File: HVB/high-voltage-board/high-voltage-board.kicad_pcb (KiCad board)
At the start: 2 copper layers, 181.6 x 105.4 mm, 69 parts, among them J1 Conn_01x23, J10 Conn_01x05, J11 HV-, J2 HECS, J3 HV+, J4 HV-, J5 HV+, J6 HV-, J7 Conn_01x02, J8 HV+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

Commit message: updating trace correction temp
changing trace and pinout of a temp wire
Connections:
- U5 pad 17: unconnected-(U5-Pad17) -> /TEMP-
- U5 pad 29: /TEMP- -> unconnected-(U5-Pad29)
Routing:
- net /TEMP-: track 10.2 -> 11.8 mm

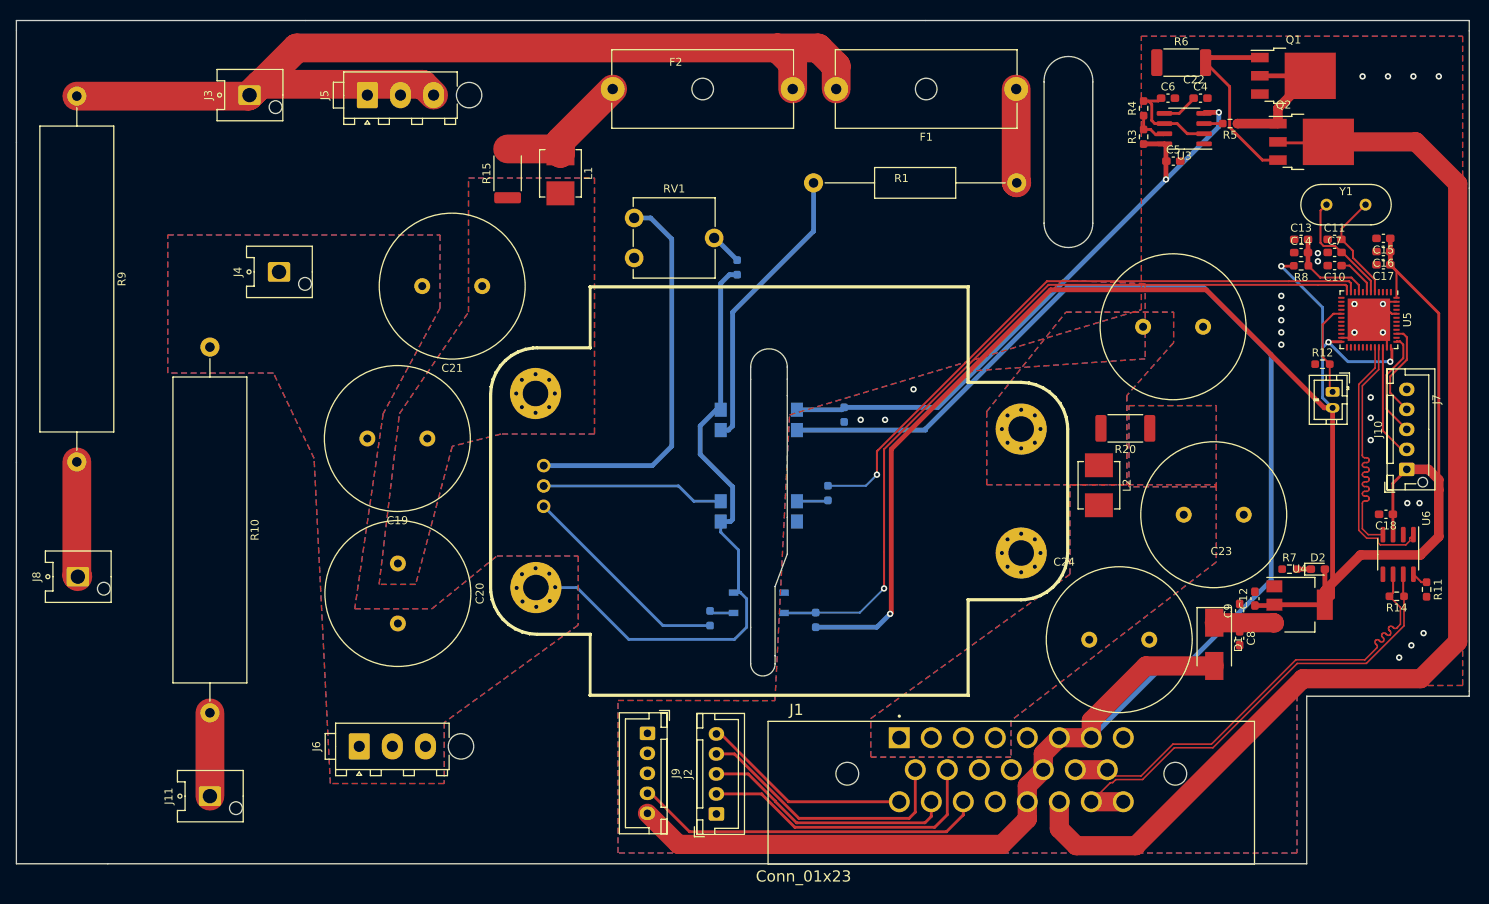
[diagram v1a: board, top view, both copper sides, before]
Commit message: adding mounting holes
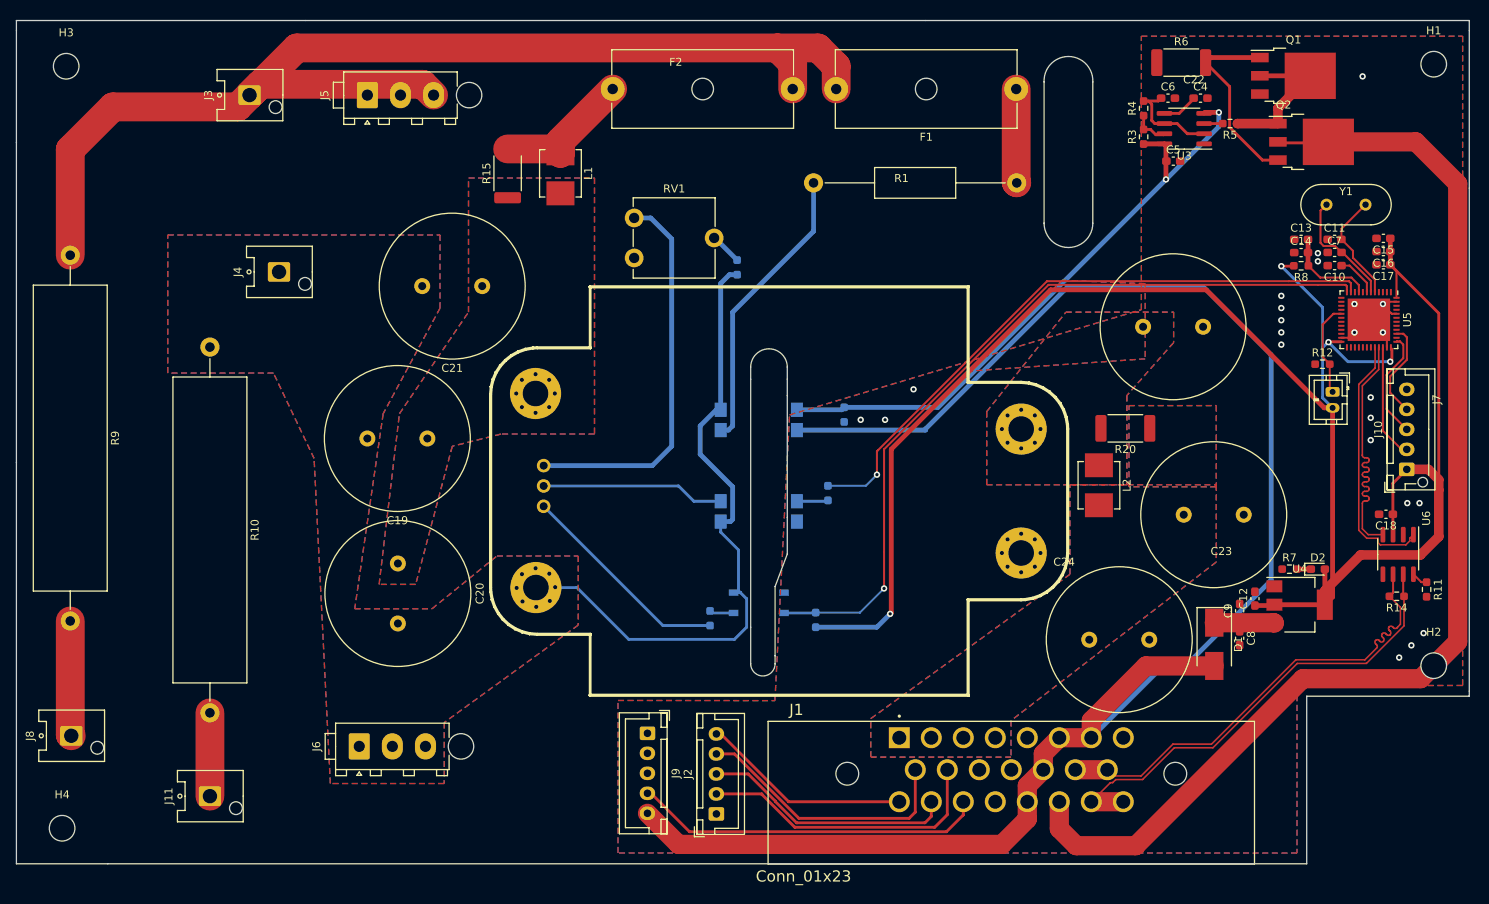
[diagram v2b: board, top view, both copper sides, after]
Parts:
- added H1: MountingHole, MountingHole:MountingHole_3.2mm_M3, F.Cu at (224.8, 44.2)
- added H2: MountingHole, MountingHole:MountingHole_3.2mm_M3, F.Cu at (224.8, 119.4)
- added H3: MountingHole, MountingHole:MountingHole_3.2mm_M3, F.Cu at (53.8, 44.5)
- added H4: MountingHole, MountingHole:MountingHole_3.2mm_M3, F.Cu at (53.3, 139.7)
- moved J8 19.9 mm to (54.5, 128.1)
- moved R9 19.9 mm to (54.4, 68.1)
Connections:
- U5 pad 10: /DC_DC_TRIM_EN -> unconnected-(U5-Pad10)
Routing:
- net HV+: track 131.3 -> 148.1 mm
- net GND: vias 26 -> 23
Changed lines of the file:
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@@
   (net 41 "unconnected-(U5-Pad4)")
   (net 42 "unconnected-(U5-Pad8)")
-  (net 43 "/DC_DC_TRIM_EN")
+  (net 43 "unconnected-(U5-Pad10)")
   (net 44 "unconnected-(U5-Pad42)")
   (net 45 "unconnected-(U5-Pad43)")
@@
     )
   )
+  (footprint "MountingHole:MountingHole_3.2mm_M3" (layer "F.Cu")
+    (at 53.34 139.7)
+    (descr "Mounting Hole 3.2mm, no annular, M3")
+    (tags "mounting hole 3.2mm no annular m3")
+    (property "Sheetfile" "high-voltage-board.kicad_sch")
+    (property "Sheetname" "")
+    (attr exclude_from_pos_files)
+    (fp_text reference "H4" (at 0 -4.2) (layer "F.SilkS")
+      (effects (font (size 1 1) (thickness 0.15)))
+    )
+    (fp_text value "MountingHole" (at 0 4.2) (layer "F.Fab")
+      (effects (font (size 1 1) (thickness 0.15)))
+    )
+    (fp_text user "${REFERENCE}" (at 0.3 0) (layer "F.Fab")
+      (effects (font (size 1 1) (thickness 0.15)))
+    )
+    (fp_circle (center 0 0) (end 3.2 0) (layer "Cmts.User") (width 0.15) (fill none))
+    (fp_circle (center 0 0) (end 3.45 0) (layer "F.CrtYd") (width 0.05) (fill none))
+    (pad "" np_thru_hole circle (at 0 0) (size 3.2 3.2) (drill 3.2) (layers *.Cu *.Mask))
+  )
   (footprint "Connector_Hirose:Hirose_DF63M-1P-3.96DSA_1x01_P3.96mm_Vertical" (layer "F.Cu")
     (at 71.8157 135.6891 90)
@@
     )
   )
+  (footprint "MountingHole:MountingHole_3.2mm_M3" placed (layer "F.Cu")
+    (at 224.79 119.38)
+    (descr "Mounting Hole 3.2mm, no annular, M3")
+    (tags "mounting hole 3.2mm no annular m3")
+    (property "Sheetfile" "high-voltage-board.kicad_sch")
+    (property "Sheetname" "")
+    (attr exclude_from_pos_files)
+    (fp_text reference "H2" (at 0 -4.2) (layer "F.SilkS")
+      (effects (font (size 1 1) (thickness 0.15)))
+    )
+    (fp_text value "MountingHole" (at 0 4.2) (layer "F.Fab")
+      (effects (font (size 1 1) (thickness 0.15)))
+    )
+    (fp_text user "${REFERENCE}" (at 0.3 0) (layer "F.Fab")
+      (effects (font (size 1 1) (thickness 0.15)))
+    )
+    (fp_circle (center 0 0) (end 3.2 0) (layer "Cmts.User") (width 0.15) (fill none))
+    (fp_circle (center 0 0) (end 3.45 0) (layer "F.CrtYd") (width 0.05) (fill none))
+    (pad "" np_thru_hole circle (at 0 0) (size 3.2 3.2) (drill 3.2) (layers *.Cu *.Mask))
+  )
   (footprint "LED_SMD:LED_0603_1608Metric_Pad1.05x0.95mm_HandSolder" (layer "F.Cu")
     (at 210.312 107.315)
@@
     )
   )
+  (footprint "MountingHole:MountingHole_3.2mm_M3" placed (layer "F.Cu")
+    (at 53.848 44.45)
+    (descr "Mounting Hole 3.2mm, no annular, M3")
+    (tags "mounting hole 3.2mm no annular m3")
+    (property "Sheetfile" "high-voltage-board.kicad_sch")
+    (property "Sheetname" "")
+    (attr exclude_from_pos_files)
+    (fp_text reference "H3" (at 0 -4.2) (layer "F.SilkS")
+      (effects (font (size 1 1) (thickness 0.15)))
+    )
+    (fp_text value "MountingHole" (at 0 4.2) (layer "F.Fab")
+      (effects (font (size 1 1) (thickness 0.15)))
+    )
+    (fp_text user "${REFERENCE}" (at 0.3 0) (layer "F.Fab")
+      (effects (font (size 1 1) (thickness 0.15)))
+    )
+    (fp_circle (center 0 0) (end 3.2 0) (layer "Cmts.User") (width 0.15) (fill none))
+    (fp_circle (center 0 0) (end 3.45 0) (layer "F.CrtYd") (width 0.05) (fill none))
+    (pad "" np_thru_hole circle (at 0 0) (size 3.2 3.2) (drill 3.2) (layers *.Cu *.Mask))
+  )
   (footprint "Package_TO_SOT_SMD:TO-252-3_TabPin2" (layer "F.Cu")
     (at 209.5187 53.9021)
@@
     )
   )
+  (footprint "MountingHole:MountingHole_3.2mm_M3" placed (layer "F.Cu")
+    (at 224.79 44.196)
+    (descr "Mounting Hole 3.2mm, no annular, M3")
+    (tags "mounting hole 3.2mm no annular m3")
+    (property "Sheetfile" "high-voltage-board.kicad_sch")
+    (property "Sheetname" "")
+    (attr exclude_from_pos_files)
+    (fp_text reference "H1" (at 0 -4.2) (layer "F.SilkS")
+      (effects (font (size 1 1) (thickness 0.15)))
+    )
+    (fp_text value "MountingHole" (at 0 4.2) (layer "F.Fab")
+      (effects (font (size 1 1) (thickness 0.15)))
+    )
+    (fp_text user "${REFERENCE}" (at 0.3 0) (layer "F.Fab")
+      (effects (font (size 1 1) (thickness 0.15)))
+    )
+    (fp_circle (center 0 0) (end 3.2 0) (layer "Cmts.User") (width 0.15) (fill none))
+    (fp_circle (center 0 0) (end 3.45 0) (layer "F.CrtYd") (width 0.05) (fill none))
+    (pad "" np_thru_hole circle (at 0 0) (size 3.2 3.2) (drill 3.2) (layers *.Cu *.Mask))
+  )
   (footprint "Capacitor_SMD:C_0603_1608Metric_Pad1.08x0.95mm_HandSolder" (layer "F.Cu")
     (at 192.2382 56.3141)
@@
   )
   (footprint "Resistor_THT:R_Axial_Power_L38.0mm_W9.0mm_P45.72mm" (layer "F.Cu")
-    (at 55.1787 48.1861 -90)
+    (at 54.356 68.072 -90)
     (descr "Resistor, Axial_Power series, Box, pin pitch=45.72mm, 9W, length*width*height=38*9*9mm^3, http://cdn-reichelt.de/documents/datenblatt/B400/5WAXIAL_9WAXIAL_11WAXIAL_17WAXIAL%23YAG.pdf")
     (tags "Resistor Axial_Power series Box pin pitch 45.72mm 9W length 38mm width 9mm height 9mm")
@@
       (net 11 "Net-(C13-Pad2)") (pinfunction "VDDA") (pintype "power_in"))
     (pad "10" smd roundrect (at -3.45 1.75 270) (size 0.8 0.25) (layers "F.Cu" "F.Paste" "F.Mask") (roundrect_rratio 0.25)
-      (net 43 "/DC_DC_TRIM_EN") (pinfunction "PA0") (pintype "bidirectional"))
+      (net 43 "unconnected-(U5-Pad10)") (pinfunction "PA0") (pintype "bidirectional"))
     (pad "11" smd roundrect (at -3.45 2.25 270) (size 0.8 0.25) (layers "F.Cu" "F.Paste" "F.Mask") (roundrect_rratio 0.25)
       (net 35 "/DC_DC_EN") (pinfunction "PA1") (pintype "bidirectional"))
@@
   )
   (footprint "Connector_Hirose:Hirose_DF63M-1P-3.96DSA_1x01_P3.96mm_Vertical" (layer "F.Cu")
-    (at 55.3057 108.2571 90)
+    (at 54.483 128.143 90)
     (descr "Hirose DF63 through hole, DF63M-1P-3.96DSA, 1 Pins per row (https://www.hirose.com/product/en/products/DF63/), generated with kicad-footprint-generator")
     (tags "connector Hirose DF63 vertical")
@@
   (segment (start 218.9377 79.5876) (end 218.9377 78.6876) (width 0.254) (layer "F.Cu") (net 2))
   (segment (start 219.5377 75.3876) (end 219.0877 74.9376) (width 0.254) (layer "F.Cu") (net 2))
-  (via (at 222.25 45.72) (size 0.8) (drill 0.4) (layers "F.Cu" "B.Cu") (free) (net 2))
   (via (at 218.44 74.168) (size 0.8) (drill 0.4) (layers "F.Cu" "B.Cu") (net 2))
   (via (at 223.52 115.316) (size 0.8) (drill 0.4) (layers "F.Cu" "B.Cu") (free) (net 2))
@@
   (via (at 205.74 79.248) (size 0.8) (drill 0.4) (layers "F.Cu" "B.Cu") (free) (net 2))
   (via (at 218.44 77.724) (size 0.8) (drill 0.4) (layers "F.Cu" "B.Cu") (net 2))
-  (via (at 219.075 45.72) (size 0.8) (drill 0.4) (layers "F.Cu" "B.Cu") (free) (net 2))
   (via (at 214.884 74.168) (size 0.8) (drill 0.4) (layers "F.Cu" "B.Cu") (net 2))
   (via (at 215.9 45.72) (size 0.8) (drill 0.4) (layers "F.Cu" "B.Cu") (free) (net 2))
@@
   (via (at 205.74 73.152) (size 0.8) (drill 0.4) (layers "F.Cu" "B.Cu") (free) (net 2))
   (via (at 216.916 88.392) (size 0.8) (drill 0.4) (layers "F.Cu" "B.Cu") (free) (net 2))
-  (via (at 225.425 45.72) (size 0.8) (drill 0.4) (layers "F.Cu" "B.Cu") (free) (net 2))
   (via (at 153.162 88.646) (size 0.8) (drill 0.4) (layers "F.Cu" "B.Cu") (free) (net 2))
   (via (at 156.21 88.646) (size 0.8) (drill 0.4) (layers "F.Cu" "B.Cu") (free) (net 2))
@@
   (segment (start 137.7188 70.5085) (end 136.7555 70.5085) (width 0.6) (layer "B.Cu") (net 61))
   (segment (start 138.1417 110.2521) (end 137.8877 109.9981) (width 0.36) (layer "B.Cu") (net 61))
-  (segment (start 55.1787 48.1861) (end 76.6417 48.1861) (width 3.6) (layer "F.Cu") (net 62))
+  (segment (start 59.69 49.53) (end 54.356 54.864) (width 3.6) (layer "F.Cu") (net 62))
   (segment (start 82.6638 42.164) (end 142.748 42.164) (width 3.6) (layer "F.Cu") (net 62))
+  (segment (start 54.356 54.864) (end 54.356 68.072) (width 3.6) (layer "F.Cu") (net 62))
   (segment (start 99.7757 48.0601) (end 98.425179 46.709579) (width 3.6) (layer "F.Cu") (net 62))
-  (segment (start 76.6417 48.1861) (end 76.7687 48.0591) (width 3.6) (layer "F.Cu") (net 62))
   (segment (start 78.118221 46.709579) (end 76.7687 48.0591) (width 3.6) (layer "F.Cu") (net 62))
   (segment (start 76.7687 48.0591) (end 82.6638 42.164) (width 3.6) (layer "F.Cu") (net 62))
   (segment (start 142.748 42.164) (end 144.6607 44.0767) (width 3.6) (layer "F.Cu") (net 62))
+  (segment (start 76.7687 48.0591) (end 75.2978 49.53) (width 3.6) (layer "F.Cu") (net 62))
   (segment (start 98.425179 46.709579) (end 78.118221 46.709579) (width 3.6) (layer "F.Cu") (net 62))
   (segment (start 144.6607 44.0767) (end 144.6607 47.2971) (width 3.6) (layer "F.Cu") (net 62))
@@
   (segment (start 142.748 42.164) (end 147.828 42.164) (width 3.6) (layer "F.Cu") (net 62))
   (segment (start 150.1007 44.4367) (end 150.1007 47.2971) (width 3.6) (layer "F.Cu") (net 62))
+  (segment (start 75.2978 49.53) (end 59.69 49.53) (width 3.6) (layer "F.Cu") (net 62))
   (segment (start 210.906289 76.748711) (end 212.2674 75.3876) (width 0.254) (layer "F.Cu") (net 63))
   (segment (start 212.2674 75.3876) (end 213.2377 75.3876) (width 0.254) (layer "F.Cu") (net 63))
@@
   (segment (start 144.92416 139.58256) (end 162.41024 139.58256) (width 0.36) (layer "F.Cu") (net 68))
   (segment (start 140.80472 135.4116) (end 140.80472 135.46312) (width 0.36) (layer "F.Cu") (net 68))
-  (segment (start 55.1787 108.1301) (end 55.3057 108.2571) (width 3.6) (layer "F.Cu") (net 74))
-  (segment (start 55.1787 93.9061) (end 55.1787 108.1301) (width 3.6) (layer "F.Cu") (net 74))
+  (segment (start 54.356 128.016) (end 54.483 128.143) (width 3.6) (layer "F.Cu") (net 74))
+  (segment (start 54.356 113.792) (end 54.356 128.016) (width 3.6) (layer "F.Cu") (net 74))
   (segment (start 71.8157 125.2751) (end 71.8157 135.6891) (width 3.6) (layer "F.Cu") (net 75))
   (segment (start 217.462699 79.612599) (end 217.4377 79.5876) (width 0.2) (layer "F.Cu") (net 77))

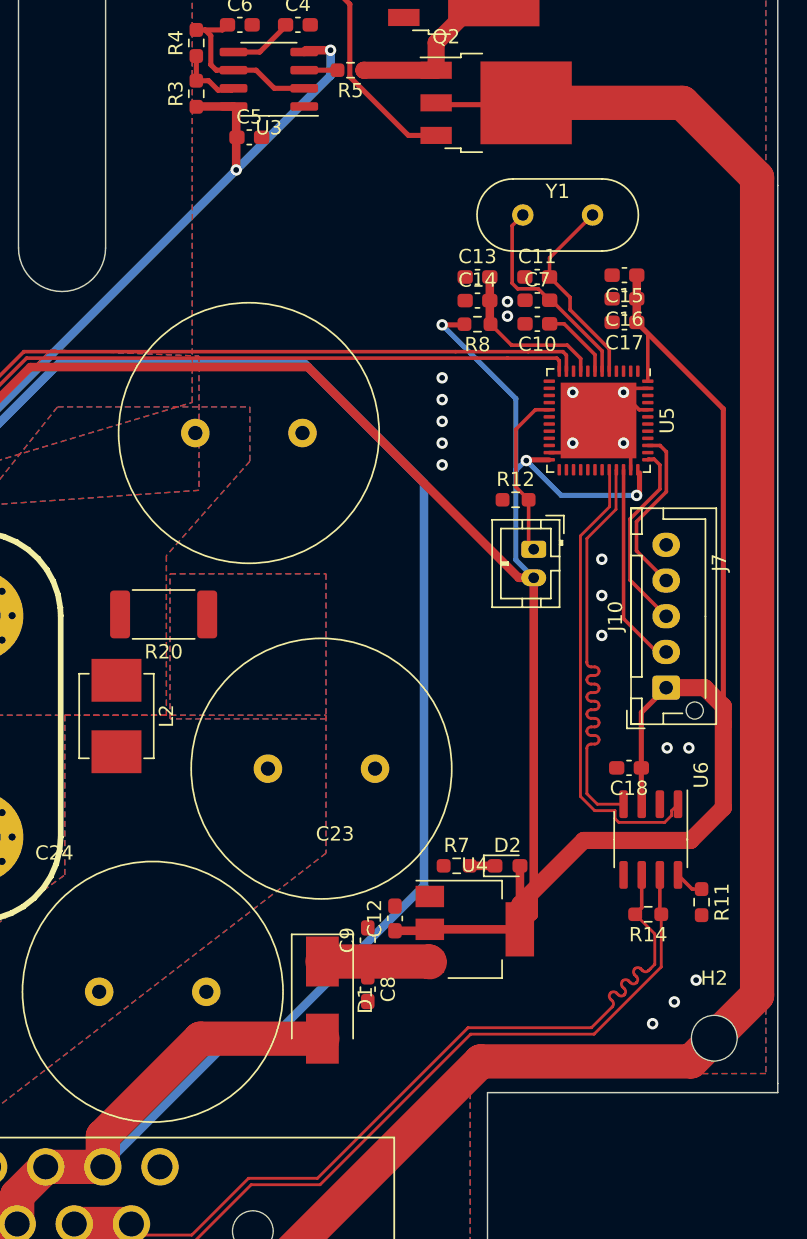
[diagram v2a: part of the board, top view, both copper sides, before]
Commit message: updating filtering cap layout
Kay suggested layout changes. Moved caps around
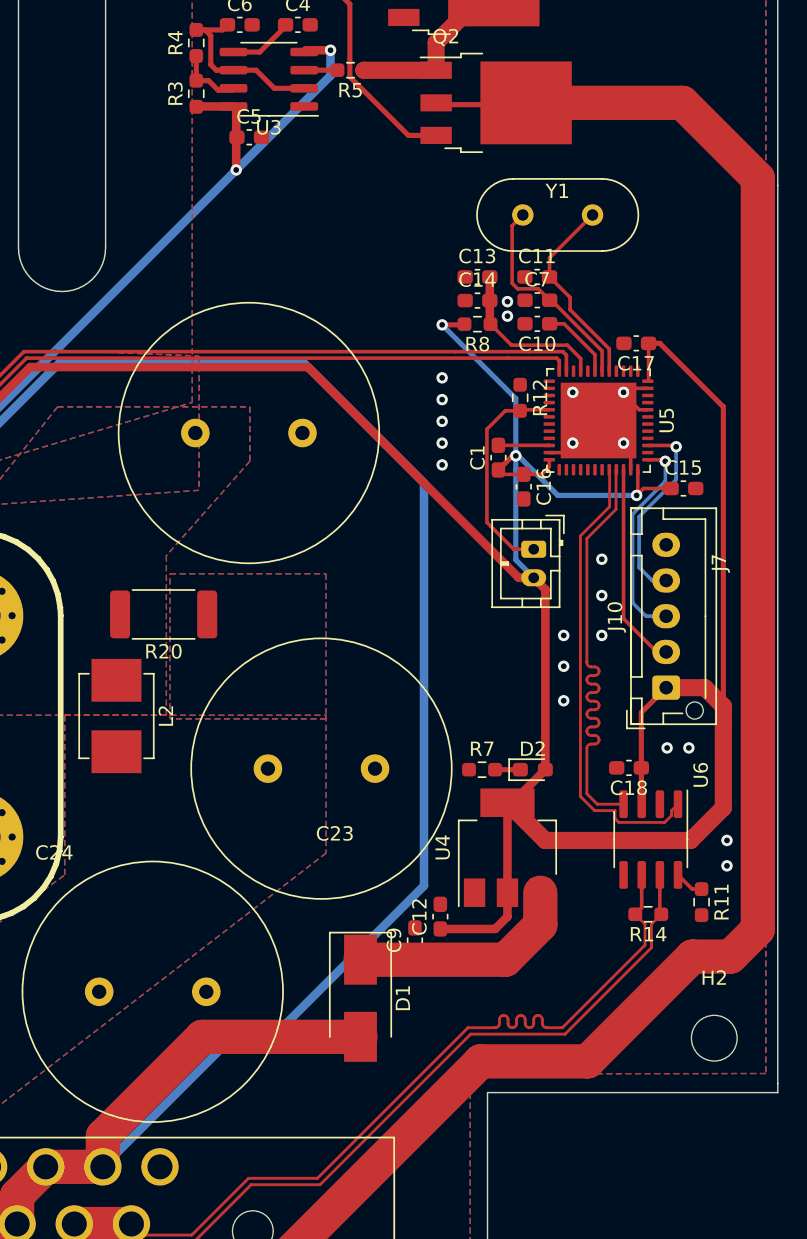
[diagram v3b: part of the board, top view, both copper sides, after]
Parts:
- removed C8: CP1, Capacitor_SMD:C_0603_1608Metric_Pad1.08x0.95mm_HandSolder
- added C1: 4.7u, Capacitor_SMD:C_0603_1608Metric_Pad1.08x0.95mm_HandSolder, F.Cu at (209.7, 78.7)
- C12: value C -> 10u
- C9: value C -> .1u
- R7: value R -> 220
- moved C15 15.5 mm to (222.6, 80.9), turned to 0 degrees
- moved C16 14.9 mm to (211.5, 80.8), turned to -90 degrees
- moved R12 7.15 mm to (211.2, 74.5), turned to -90 degrees
- moved D2 6.96 mm to (212.1, 100.6)
- moved R7 6.96 mm to (208.5, 100.6)
- moved U4 6.16 mm to (210.3, 106.0), turned to 90 degrees
- moved C9 3.30 mm to (203.8, 112.5)
- moved C12 3.18 mm to (205.6, 110.9)
- moved D1 2.67 mm to (200.0, 116.6)
- moved C17 1.69 mm to (219.3, 70.7)
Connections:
- U5 pad 22: unconnected-(U5-Pad22) -> Net-(U5-Pad22)
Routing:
- net +3V3: track 251.1 -> 242.5 mm
- net Net-(C9-Pad1): track 7.54 -> 15.8 mm
- net /TEMP-: track 11.8 -> 15.5 mm
- net Net-(U5-Pad22): track 0.00 -> 3.56 mm
- net GND: track 4.57 -> 7.84 mm, vias 23 -> 25
- net +12V: track 215.7 -> 218.4 mm
- net /TSAL_GND: track 146.5 -> 143.9 mm
- net B3_TRACESWO: track 12.2 -> 13.8 mm, vias 0 -> 1
- net A14_SWCLK: track 13.5 -> 14.9 mm, vias 0 -> 1
- net /CAN-: track 58.8 -> 57.6 mm
- net /CAN+: track 58.7 -> 57.5 mm

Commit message: DRC and Labeling Complete
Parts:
- added G***: LOGO, AERO_Footprints:hvlightningsymbol, F.Cu at (64.8, 68.1)
- added G***: LOGO, AERO_Footprints:AERO_Logo_15x6mm, F.Cu at (87.4, 140.7)
- added G***: LOGO, AERO_Footprints:hvlightningsymbol, B.Cu at (89.6, 67.8)
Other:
- board size 181.6 x 105.4 mm -> 181.6 x 106 mm
- board text added: "G.Spearing 22.032"
- board text added: "GLV"
- board text added: "HIGH VOLTAGE"
- board text added: "M3 Hole"
- board text added: "TSV"
